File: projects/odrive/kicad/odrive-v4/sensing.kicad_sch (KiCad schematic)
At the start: 67 parts, among them U10 TLV9062, U11 TMUX1204, U12 TLV7031, U13 TLV431, U14 74LVC1G04, U15 74LVC1G08

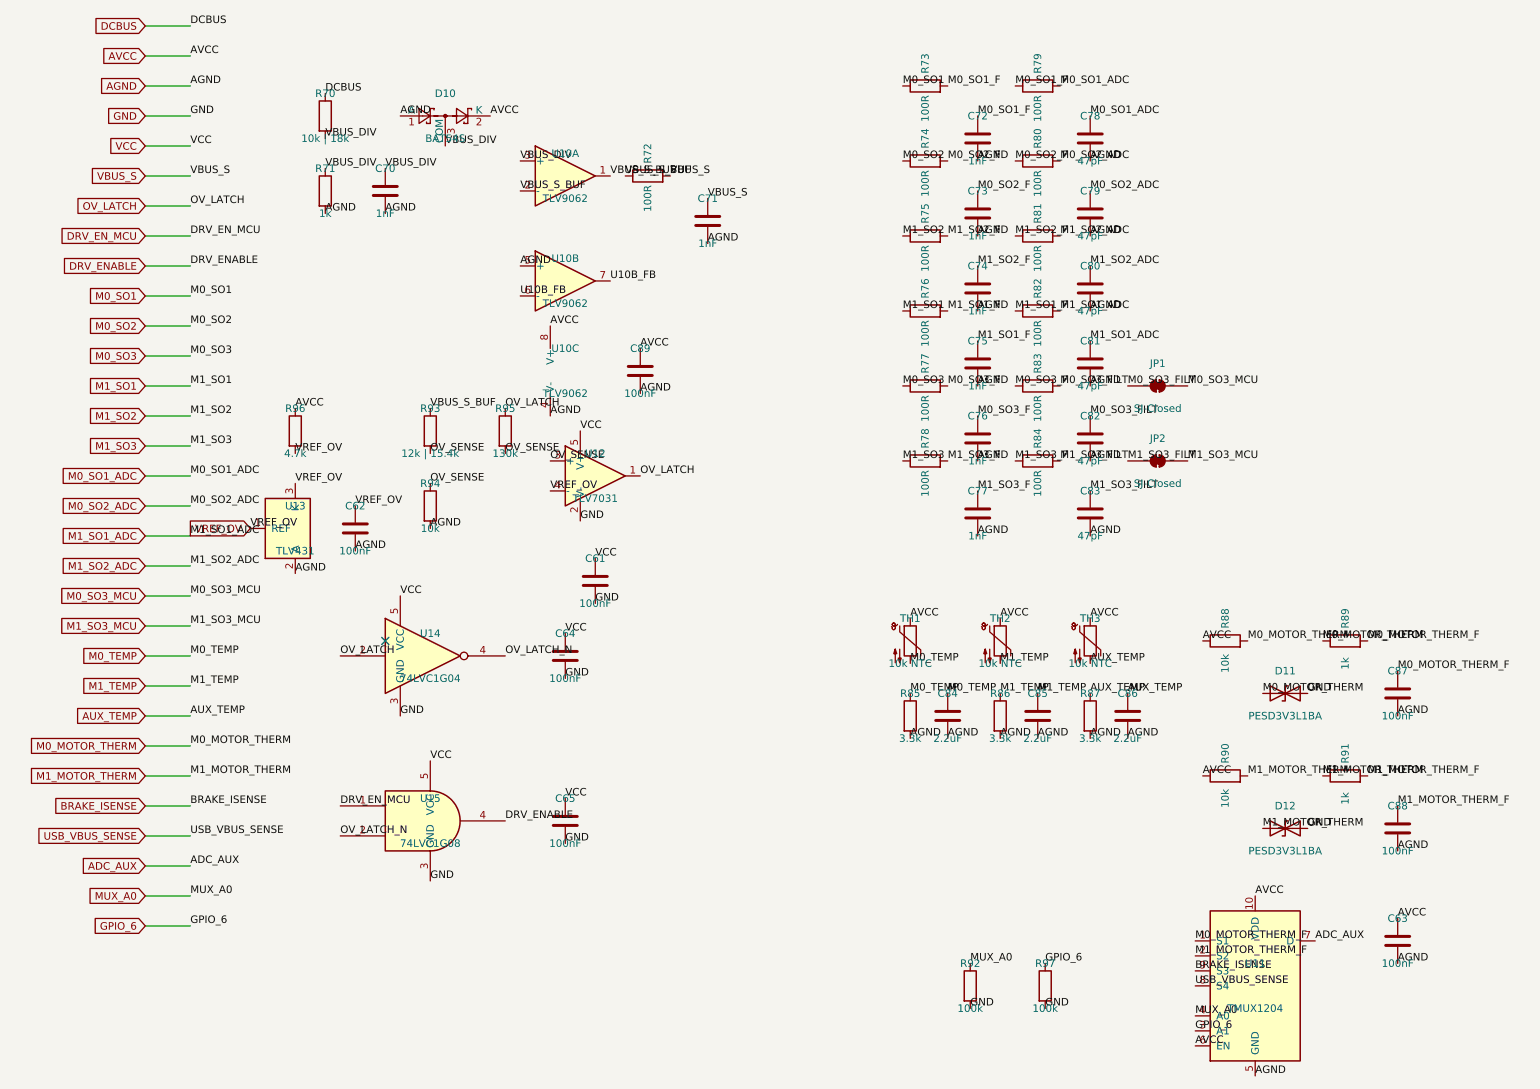
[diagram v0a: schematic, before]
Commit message: Make the v4 schematic sheets readable, netlist-invariant
The verified v4 schematic was electrically perfect and visually unreadable:
connectivity lived in labels stuck on pins, text overlapped, and parts sat
on the title block. Reworked all ten block sheets through Konnect: real
wires for local connections, labels kept for power rails and inter-sheet
nets, parts grouped by function, junction dots where wires join.

The invariant was enforced, not assumed: the exported netlist is diffed
against a reference frozen before the rework - 378 components and 283 nets,
identical membership pin by pin - and ERC holds at 0 errors. The lesson
that forced the rework is now a standing gate: numeric oracles (ERC,
netlist diff, overlap counts) all passed on the unreadable version, so
every sheet is also rendered to PNG and looked at before being declared
done.

An interrupted fix round left one known cosmetic issue, documented in
docs/LOG.md: the encoders-gpio GPIO group's reference/value text fields
float ~134mm right of their symbols, over the title block. konnect 0.2.2
has no tool that repositions property fields, so it waits for 0.11.0.
Also adds the fab footprints the sheets reference (MEGA fuse, Phoenix
terminal blocks, CMC) and restores the board file to the blank template -
the aborted layout skeleton was not worth keeping.
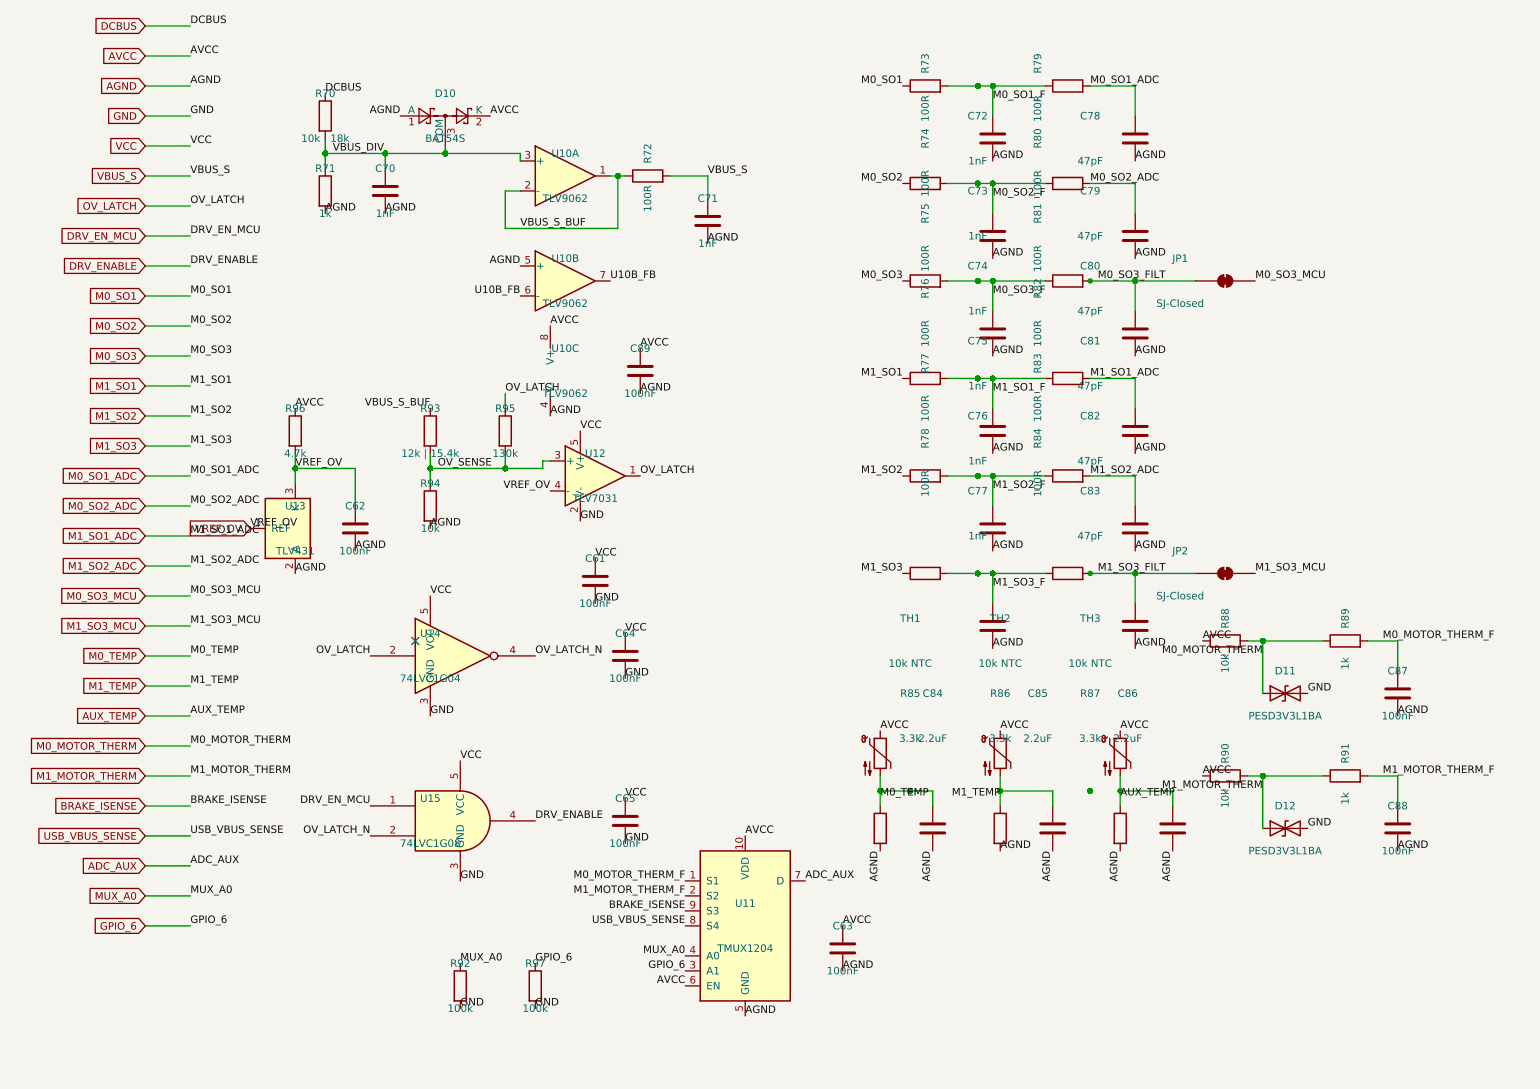
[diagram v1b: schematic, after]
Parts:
- C61, C62, C63, C64, C65, C70, C71, C72, C73, C74, C75, C76, C77, C78, C79, C80, C81, C82, C83, C84, C85, C86, C87, C88, C89: footprint (none) -> Capacitor_SMD:C_0603_1608Metric
- D10, U13: footprint (none) -> Package_TO_SOT_SMD:SOT-23
- D11, D12: footprint (none) -> Diode_SMD:D_SOD-323
- JP1, JP2: footprint (none) -> Jumper:SolderJumper-2_P1.3mm_Bridged_RoundedPad1.0x1.5mm
- R70, R71, R72, R73, R74, R75, R76, R77, R78, R79, R80, R81, R82, R83, R84, R85, R86, R87, R88, R89, R90, R91, R92, R93, R94, R95, R96, R97, TH1, TH2, TH3: footprint (none) -> Resistor_SMD:R_0603_1608Metric
- U10: footprint (none) -> Package_SO:SOIC-8_3.9x4.9mm_P1.27mm
- U11: footprint (none) -> Package_SO:MSOP-10_3x3mm_P0.5mm
- U12, U14, U15: footprint (none) -> Package_TO_SOT_SMD:SOT-23-5
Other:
- moved on the sheet: C63, C64, C65, C72, C73, C74, C75, C76, C77, C78, C79, C80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

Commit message: Import the v4 netlist onto a 4-layer board, checkpoint before placement
update_pcb_from_schematic (konnect 0.11.0, live IPC, single undo commit)
lands all 378 footprints with 283 nets and zero conflicts. Getting there
took three tries worth of fixes, all kept: the project fp-lib-table now
registers the 18 standard footprint libraries the sheets reference (the
kicad wrapper's KICAD10_FOOTPRINT_DIR is invisible to project resolution,
same story as the symbol libraries); the seven current shunts move to the
real R_Shunt_Vishay_WSK2512_6332Metric_T2.66mm kelvin footprint (the
T1_T2 name the builder invented does not exist); the OV-latch 74LVC1G74
moves to TSSOP-8 (no DCU footprint in this library snapshot - order the
DCT variant); and the SO3 solder jumpers drop the RoundedPad variant
whose custom-shape pads KiCad 10's typed IPC placement path refuses.
Board outline 120x80mm rounded, In1/In2.Cu added file-based after
learning that adding them with pcbnew open gets clobbered by its next
save. Placement not started - components sit stacked at the import
default.
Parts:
- JP1, JP2: footprint Jumper:SolderJumper-2_P1.3mm_Bridged_RoundedPad1.0x1.5mm -> Jumper:SolderJumper-2_P1.3mm_Bridged_Pad1.0x1.5mm
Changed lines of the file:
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@@
         (font
           (size 1.27 1.27))))
-    (property "Footprint" "Jumper:SolderJumper-2_P1.3mm_Bridged_RoundedPad1.0x1.5mm"
+    (property "Footprint" "Jumper:SolderJumper-2_P1.3mm_Bridged_Pad1.0x1.5mm"
       (at 190.5 63.5 0)
       (hide yes)
@@
         (font
           (size 1.27 1.27))))
-    (property "Footprint" "Jumper:SolderJumper-2_P1.3mm_Bridged_RoundedPad1.0x1.5mm"
+    (property "Footprint" "Jumper:SolderJumper-2_P1.3mm_Bridged_Pad1.0x1.5mm"
       (at 190.5 113.03 0)
       (hide yes)
